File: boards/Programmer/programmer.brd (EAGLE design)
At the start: 16.2 x 14.5 mm, 2 parts

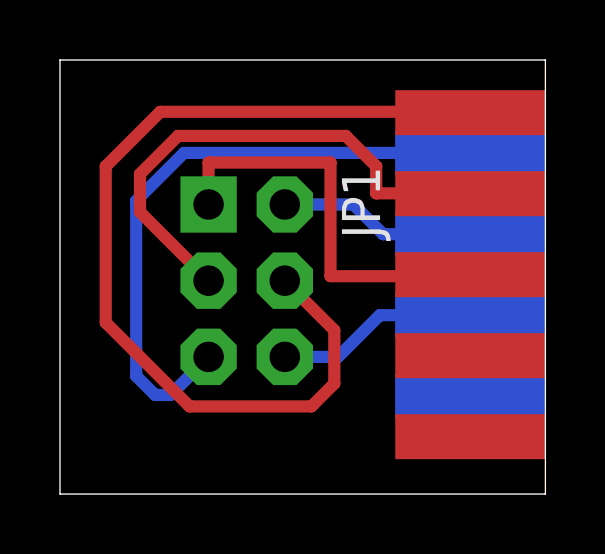
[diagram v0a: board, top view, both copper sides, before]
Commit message: Updated programmer board to match BB2 Pinouts.
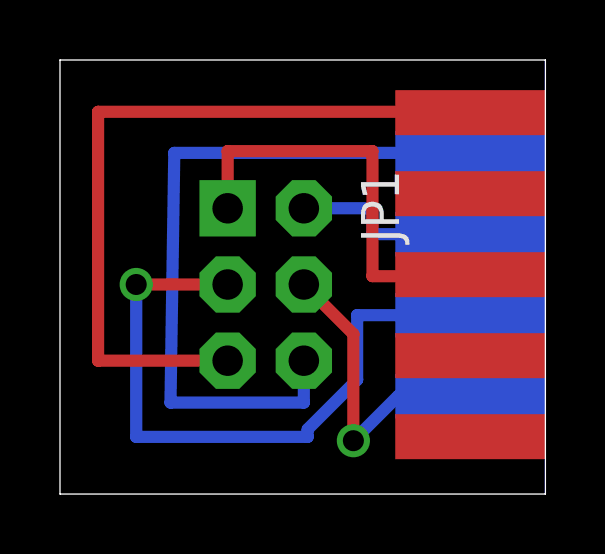
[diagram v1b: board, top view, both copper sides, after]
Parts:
- moved JP1 0.65 mm to (6.86, 6.99)
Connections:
- net VDD renamed VCC
- net GND: now also U$1.P$6; no longer U$1.P$8
- net MOSI: now also U$1.P$9; no longer U$1.P$1
- net RESET: now also U$1.P$1; no longer U$1.P$6
- net SCK: now also U$1.P$8; no longer U$1.P$2
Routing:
- net MOSI: track 32.9 -> 11.1 mm, vias 0 -> 1
- net GND: track 7.53 -> 24.9 mm
- net RESET: track 21.7 -> 26.6 mm
- net SCK: track 18.8 -> 23.1 mm, vias 0 -> 1
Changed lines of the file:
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@@
 </autorouter>
 <elements>
-<element name="JP1" library="SparkFun-Connectors" package="2X3-NS" value="AVR_SPI_PRG_6NS" x="6.223" y="7.112" rot="R270"/>
+<element name="JP1" library="SparkFun-Connectors" package="2X3-NS" value="AVR_SPI_PRG_6NS" x="6.858" y="6.985" rot="R270"/>
 <element name="U$1" library="custom" package="FOUR" value="DSUB" x="11.176" y="13.462" rot="R270"/>
 </elements>
 <signals>
-<signal name="VDD">
-<contactref element="JP1" pad="2"/>
-<contactref element="U$1" pad="P$7"/>
-<wire x1="14.486" y1="8.662" x2="10.769" y2="8.662" width="0.4064" layer="16"/>
-<wire x1="10.769" y1="8.662" x2="9.779" y2="9.652" width="0.4064" layer="16"/>
-<wire x1="9.779" y1="9.652" x2="7.493" y2="9.652" width="0.4064" layer="16"/>
-</signal>
-<signal name="GND">
-<contactref element="JP1" pad="6"/>
-<contactref element="U$1" pad="P$8"/>
-<wire x1="7.493" y1="4.572" x2="9.271" y2="4.572" width="0.4064" layer="16"/>
-<wire x1="9.271" y1="4.572" x2="10.661" y2="5.962" width="0.4064" layer="16"/>
-<wire x1="10.661" y1="5.962" x2="14.446" y2="5.962" width="0.4064" layer="16"/>
-</signal>
-<signal name="MOSI">
-<contactref element="JP1" pad="4"/>
+<signal name="RESET">
 <contactref element="U$1" pad="P$1"/>
-<wire x1="7.493" y1="7.112" x2="9.144" y2="5.461" width="0.4064" layer="1"/>
-<wire x1="9.144" y1="5.461" x2="9.144" y2="3.683" width="0.4064" layer="1"/>
-<wire x1="9.144" y1="3.683" x2="8.382" y2="2.921" width="0.4064" layer="1"/>
-<wire x1="8.382" y1="2.921" x2="4.318" y2="2.921" width="0.4064" layer="1"/>
-<wire x1="4.318" y1="2.921" x2="1.524" y2="5.715" width="0.4064" layer="1"/>
-<wire x1="1.524" y1="5.715" x2="1.524" y2="10.922" width="0.4064" layer="1"/>
-<wire x1="1.524" y1="10.922" x2="3.344" y2="12.742" width="0.4064" layer="1"/>
-<wire x1="3.344" y1="12.742" x2="15.276" y2="12.742" width="0.4064" layer="1"/>
+<contactref element="JP1" pad="5"/>
+<wire x1="5.588" y1="4.445" x2="1.27" y2="4.445" width="0.4064" layer="1"/>
+<wire x1="1.27" y1="4.445" x2="1.27" y2="12.742" width="0.4064" layer="1"/>
+<wire x1="1.27" y1="12.742" x2="15.276" y2="12.742" width="0.4064" layer="1"/>
 </signal>
 <signal name="MISO">
 <contactref element="JP1" pad="1"/>
 <contactref element="U$1" pad="P$3"/>
-<wire x1="4.953" y1="9.652" x2="4.953" y2="11.049" width="0.4064" layer="1"/>
-<wire x1="4.953" y1="11.049" x2="9.017" y2="11.049" width="0.4064" layer="1"/>
-<wire x1="9.017" y1="11.049" x2="9.017" y2="7.262" width="0.4064" layer="1"/>
-<wire x1="9.017" y1="7.262" x2="15.076" y2="7.262" width="0.4064" layer="1"/>
+<wire x1="5.588" y1="9.525" x2="5.588" y2="11.43" width="0.4064" layer="1"/>
+<wire x1="5.588" y1="11.43" x2="10.414" y2="11.43" width="0.4064" layer="1"/>
+<wire x1="10.414" y1="11.43" x2="10.414" y2="7.262" width="0.4064" layer="1"/>
+<wire x1="10.414" y1="7.262" x2="15.076" y2="7.262" width="0.4064" layer="1"/>
+</signal>
+<signal name="GND">
+<contactref element="U$1" pad="P$6"/>
+<contactref element="JP1" pad="6"/>
+<wire x1="8.128" y1="4.445" x2="8.128" y2="3.048" width="0.4064" layer="16"/>
+<wire x1="8.128" y1="3.048" x2="3.683" y2="3.048" width="0.4064" layer="16"/>
+<wire x1="3.683" y1="3.048" x2="3.81" y2="11.372" width="0.4064" layer="16"/>
+<wire x1="3.81" y1="11.372" x2="14.546" y2="11.372" width="0.4064" layer="16"/>
+</signal>
+<signal name="VCC">
+<contactref element="U$1" pad="P$7"/>
+<contactref element="JP1" pad="2"/>
+<wire x1="8.128" y1="9.525" x2="10.414" y2="9.525" width="0.4064" layer="16"/>
+<wire x1="10.414" y1="9.525" x2="10.414" y2="8.662" width="0.4064" layer="16"/>
+<wire x1="10.414" y1="8.662" x2="14.486" y2="8.662" width="0.4064" layer="16"/>
 </signal>
 <signal name="SCK">
+<contactref element="U$1" pad="P$8"/>
 <contactref element="JP1" pad="3"/>
-<contactref element="U$1" pad="P$2"/>
-<wire x1="4.953" y1="7.112" x2="2.667" y2="9.398" width="0.4064" layer="1"/>
-<wire x1="2.667" y1="9.398" x2="2.667" y2="10.668" width="0.4064" layer="1"/>
-<wire x1="2.667" y1="10.668" x2="3.937" y2="11.938" width="0.4064" layer="1"/>
-<wire x1="3.937" y1="11.938" x2="9.525" y2="11.938" width="0.4064" layer="1"/>
-<wire x1="9.525" y1="11.938" x2="10.541" y2="10.922" width="0.4064" layer="1"/>
-<wire x1="10.541" y1="10.922" x2="10.541" y2="10.022" width="0.4064" layer="1"/>
-<wire x1="10.541" y1="10.022" x2="15.146" y2="10.022" width="0.4064" layer="1"/>
+<wire x1="5.588" y1="6.985" x2="2.54" y2="6.985" width="0.4064" layer="1"/>
+<via x="2.54" y="6.985" extent="1-16" drill="0.7" shape="square"/>
+<wire x1="2.54" y1="6.985" x2="2.54" y2="1.905" width="0.4064" layer="16"/>
+<wire x1="2.54" y1="1.905" x2="8.255" y2="1.905" width="0.4064" layer="16"/>
+<wire x1="8.255" y1="1.905" x2="8.255" y2="2.159" width="0.4064" layer="16"/>
+<wire x1="8.255" y1="2.159" x2="9.906" y2="3.81" width="0.4064" layer="16"/>
+<wire x1="9.906" y1="3.81" x2="9.906" y2="5.962" width="0.4064" layer="16"/>
+<wire x1="9.906" y1="5.962" x2="14.446" y2="5.962" width="0.4064" layer="16"/>
 </signal>
-<signal name="RESET">
-<contactref element="JP1" pad="5"/>
-<contactref element="U$1" pad="P$6"/>
-<wire x1="4.953" y1="4.572" x2="3.683" y2="3.302" width="0.4064" layer="16"/>
-<wire x1="3.683" y1="3.302" x2="3.175" y2="3.302" width="0.4064" layer="16"/>
-<wire x1="3.175" y1="3.302" x2="2.54" y2="3.937" width="0.4064" layer="16"/>
-<wire x1="2.54" y1="3.937" x2="2.54" y2="9.779" width="0.4064" layer="16"/>
-<wire x1="2.54" y1="9.779" x2="4.133" y2="11.372" width="0.4064" layer="16"/>
-<wire x1="4.133" y1="11.372" x2="14.546" y2="11.372" width="0.4064" layer="16"/>
+<signal name="MOSI">
+<contactref element="U$1" pad="P$9"/>
+<contactref element="JP1" pad="4"/>
+<wire x1="8.128" y1="6.985" x2="9.779" y2="5.334" width="0.4064" layer="1"/>
+<wire x1="9.779" y1="5.334" x2="9.779" y2="1.778" width="0.4064" layer="1"/>
+<via x="9.779" y="1.778" extent="1-16" drill="0.7" shape="square"/>
+<wire x1="9.779" y1="1.778" x2="11.273" y2="3.272" width="0.4064" layer="16"/>
+<wire x1="11.273" y1="3.272" x2="14.376" y2="3.272" width="0.4064" layer="16"/>
 </signal>
 </signals>
